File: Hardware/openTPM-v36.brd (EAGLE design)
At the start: 45 x 19 mm, 69 parts, among them U1 SAM4S4A, U2 TPS62172, U3 TC58CVG0S3HQAIEWSON, Y1 12MHZ, Y2 32KHz

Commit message: v36
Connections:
- new net N$19: U1.22, U3.1
- new net N$24: U1.27, U3.7
- new net N$25: U1.26, U3.3
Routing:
- net N$19: track 0.00 -> 23.0 mm, vias 0 -> 2
- net N$25: track 0.00 -> 18.9 mm, vias 0 -> 1
- net N$24: track 0.00 -> 17.1 mm, vias 0 -> 1
- net ECC: track 12.3 -> 11.7 mm
- net AES: track 17.8 -> 17.2 mm

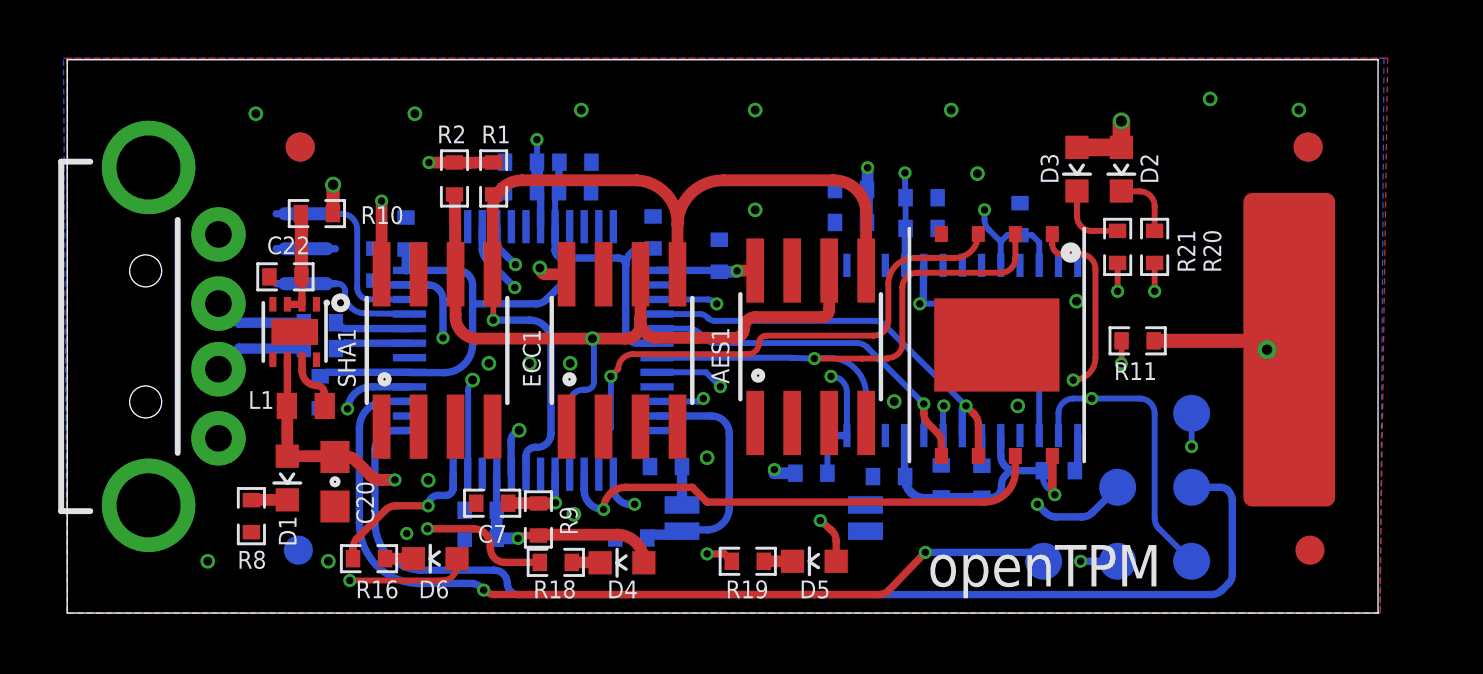
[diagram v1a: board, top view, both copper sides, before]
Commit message: cleaned silk up, added logo and binary words.
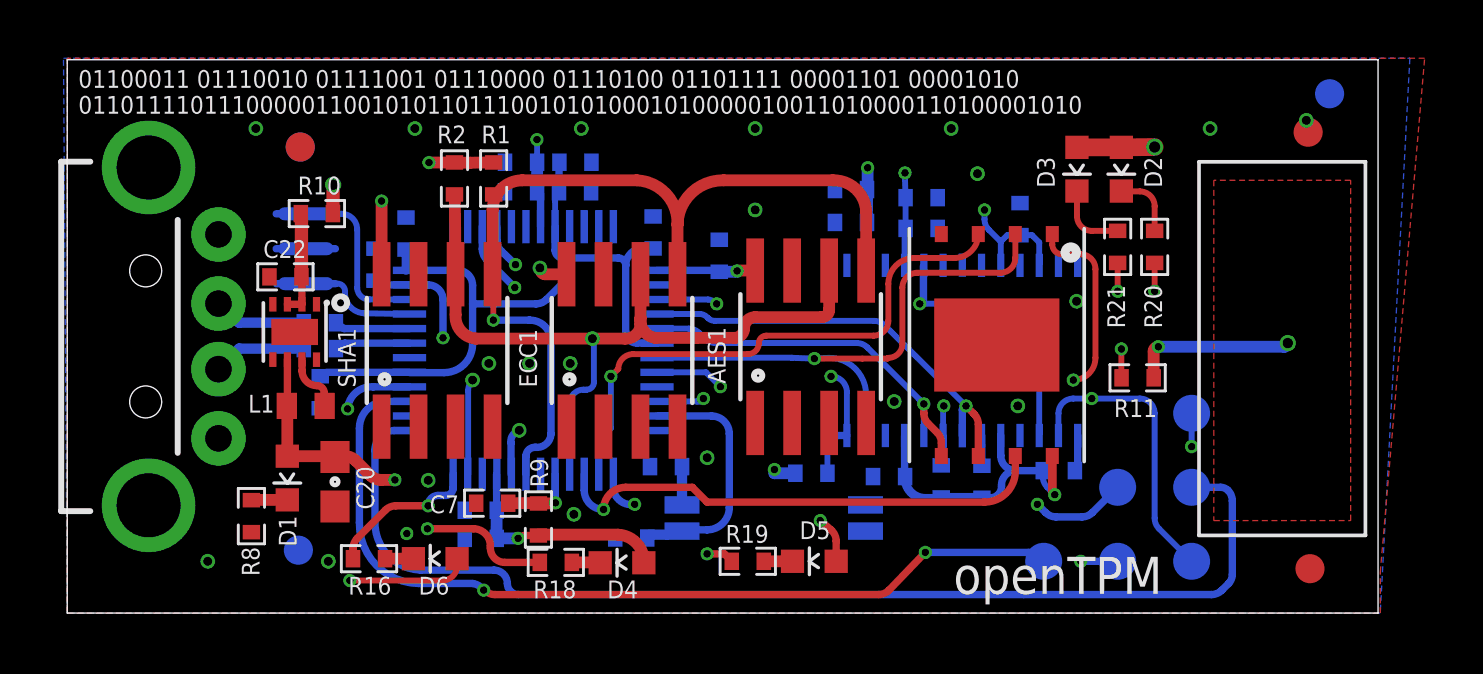
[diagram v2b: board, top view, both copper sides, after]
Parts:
- removed SL1: SLIDER_PASSIVE_1SEG, u2ftoken:SLIDER_PASSIVE_1SEG_12MM
- moved FID6 1.97 mm to (43.3, 17.8)
- moved R11 1.27 mm to (36.8, 8.08)
- moved FID3 0.63 mm to (42.7, 1.52)
- moved FID1 0.51 mm to (42.6, 16.5)
- renumbered TP1 to RST, TP2 to SWCLK, TP3 to SWDIO, TP4 to PB5, TP5 to PB4, TP6 to 3V3
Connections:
- net N$3 renamed PB4
- net N$4 renamed PB5
- net N$5 renamed SWDIO
- net N$6 renamed SWCLK
- removed net N$7: R11.2, SL1.S1
- new net CAP: R11.2
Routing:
- net CAP: track 0.00 -> 5.66 mm, vias 0 -> 2
- net N$7: track 3.99 -> 0.00 mm
- added copper zone on layer 1, net CAP
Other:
- board text added: "01100011 01110010 01111001 01110000 01110100 01101111 00001101 00001010"
- board text added: "01101111 01110000 01100101 01101110 01010100 01010000 01001101 00001101 00001010"
- board text added: "011011110111000001100101011011100101010001010000010011010000110100001010"
